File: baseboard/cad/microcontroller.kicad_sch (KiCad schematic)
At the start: 12 parts, among them J16 Conn_01x04_Pin, SW3 SW_DIP_x01, U1 STM32G031K8Ux, U3 ADG5434, Y1 830054236

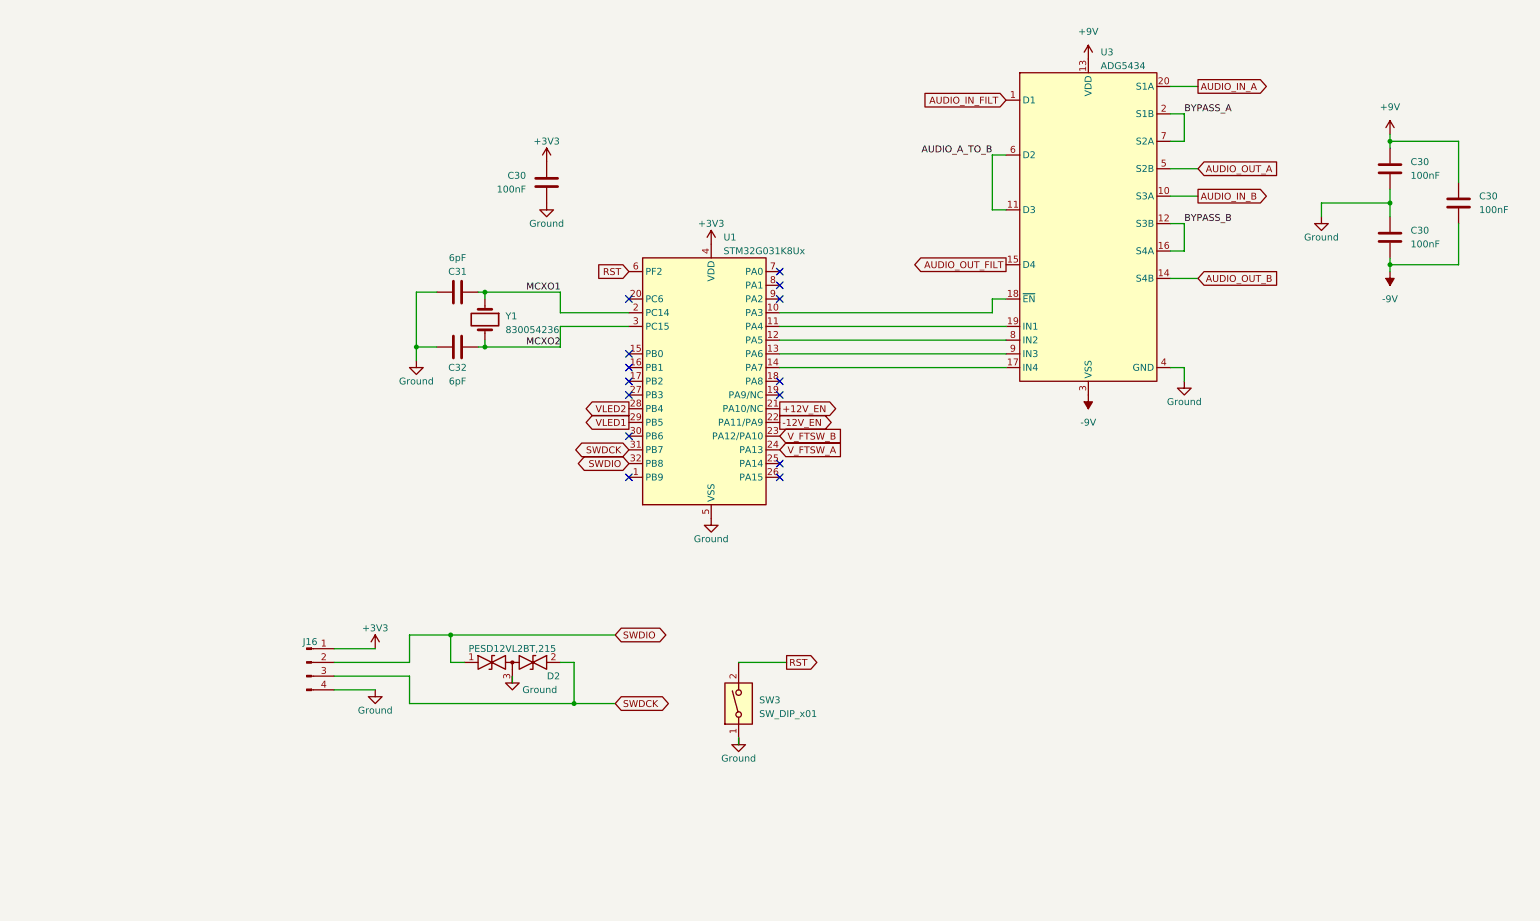
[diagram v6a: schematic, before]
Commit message: updated schematic page setup
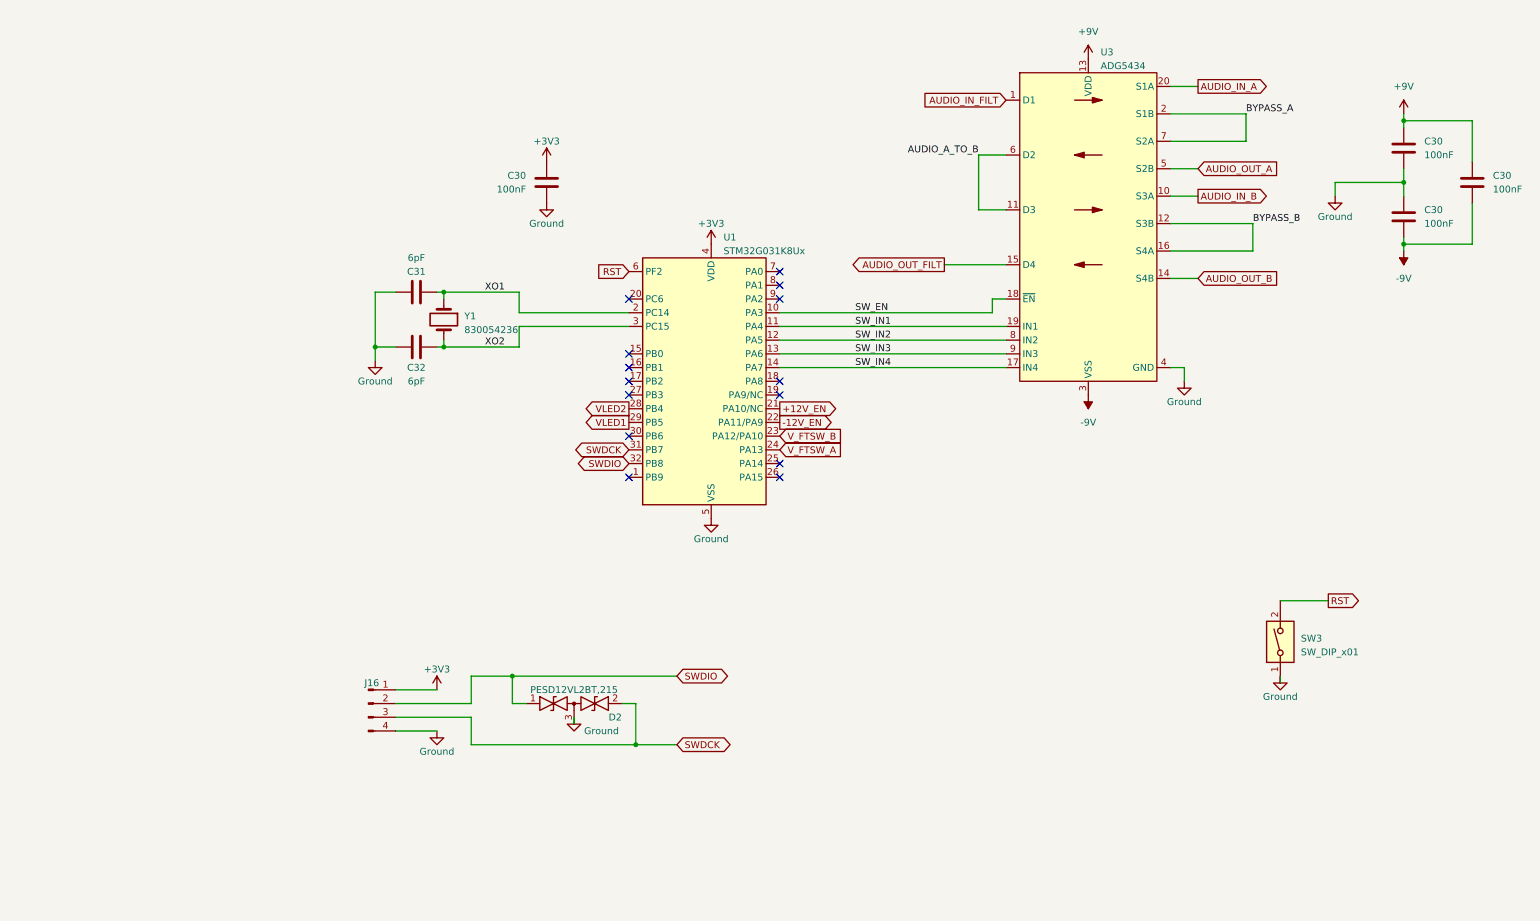
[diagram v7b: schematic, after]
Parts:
- U1: footprint Package_DFN_QFN:QFN-32-1EP_5x5mm_P0.5mm_EP3.45x3.45mm_ThermalVias -> Package_DFN_QFN:QFN-32-1EP_5x5mm_P0.5mm_EP3.45x3.45mm
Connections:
- net SW_IN4: now reaches U1.14 (PA7), U3.17 (IN4)
- net SW_EN: now reaches U1.10 (PA3), U3.18 (~{EN})
- net SW_IN1: now reaches U1.11 (PA4), U3.19 (IN1)
- net SW_IN2: now reaches U1.12 (PA5), U3.8 (IN2)
- net SW_IN3: now reaches U1.13 (PA6), U3.9 (IN3)
- net MCXO1 renamed XO1
- net MCXO2 renamed XO2
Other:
- moved on the sheet: C30, C31, C32, D2, J16, SW3, Y1

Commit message: more early layout work
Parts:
- U1: footprint Package_DFN_QFN:QFN-32-1EP_5x5mm_P0.5mm_EP3.45x3.45mm -> Package_DFN_QFN:QFN-32-1EP_5x5mm_P0.5mm_EP3.45x3.45mm_ThermalVias
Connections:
- net SW_EN: no longer names the net of U3.18 (~{EN})
- net SW_EN: now also U1.13 (PA6); no longer U1.10 (PA3)
- net SW_IN1: no longer names the net of U3.19 (IN1)
- net SW_IN1: now also U1.12 (PA5); no longer U1.11 (PA4)
- net SW_IN2: no longer names the net of U3.8 (IN2)
- net SW_IN2: now also U1.10 (PA3); no longer U1.12 (PA5)
- net SW_IN3: no longer names the net of U3.9 (IN3)
- net SW_IN3: now also U1.11 (PA4); no longer U1.13 (PA6)
- net SW_IN4: no longer names the net of U1.14 (PA7), U3.17 (IN4)
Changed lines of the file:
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@@
-    (effects (font (size 1.27 1.27)) (justify left bottom))
-  )
-  (label "SW_IN1" (at 129.54 93.98 0) (fields_autoplaced)
-    (effects (font (size 1.27 1.27)) (justify left bottom))
-  )
-  (label "SW_IN3" (at 129.54 99.06 0) (fields_autoplaced)
     (effects (font (size 1.27 1.27)) (justify left bottom))
   )
@@
     (effects (font (size 1.27 1.27)) (justify left bottom))
   )
-  (label "SW_EN" (at 129.54 91.44 0) (fields_autoplaced)
-    (effects (font (size 1.27 1.27)) (justify left bottom))
-  )
   (label "BYPASS_A" (at 201.93 54.61 0) (fields_autoplaced)
-    (effects (font (size 1.27 1.27)) (justify left bottom))
-  )
-  (label "SW_IN2" (at 129.54 96.52 0) (fields_autoplaced)
-    (effects (font (size 1.27 1.27)) (justify left bottom))
-  )
-  (label "SW_IN4" (at 129.54 101.6 0) (fields_autoplaced)
     (effects (font (size 1.27 1.27)) (justify left bottom))
   )
@@
       (effects (font (size 1.27 1.27)) (justify left))
     )
-    (property "Footprint" "Package_DFN_QFN:QFN-32-1EP_5x5mm_P0.5mm_EP3.45x3.45mm" (at 90.17 127 0)
+    (property "Footprint" "Package_DFN_QFN:QFN-32-1EP_5x5mm_P0.5mm_EP3.45x3.45mm_ThermalVias" (at 90.17 127 0)
       (effects (font (size 1.27 1.27)) (justify right) hide)
     )
